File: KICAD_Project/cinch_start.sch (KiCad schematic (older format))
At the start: 14 parts, among them P10 CONN_1, P11 CONN_1, P12 CONN_1, P13 CONN_1, P14 CONN_1, P15 CONN_1, P16 CONN_1, P6 CONN_1, P7 CONN_1, P8 CONN_1, P9 CONN_1, T1 ACT45B

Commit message: Started laying out the harness in DXF, initial schematic capture complete, except for harness.
Signed-off-by: Jared Harvey <TortiseGIT@jaredharvey.com>
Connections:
- net labels added: GND_PWR4, GND_PWR5, GND_PWR6, GND_PWR7, GND_PWR8, INJ00_PIN, INJ01_PIN, INJ02_PIN, INJ03_PIN, INJ04_PIN, INJ05_PIN, INJ06_PIN, INJ07_PIN, INJ08_PIN, INJ09_PIN, INJ13_PIN, INJ14_PIN, INJ15_PIN, INJ16_PIN, INJ17_PIN, INJ18_PIN, INJ19_PIN, INJ20_PIN, INJ21_PIN, INJ22_PIN, INJ23_PIN
- wire segments 375 -> 356

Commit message: About to runs scripts to scrub the BOM's, so here's a backup copy in case it goes wrong.
Signed-off-by: Jared Harvey <TortiseGIT@jaredharvey.com>
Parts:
- R101: renamed from R1; footprint SM0805-R4 -> SM0805
- renumbered D1 to D101, P6 to P101, P7 to P102, P8 to P103, P9 to P104, P10 to P105, P11 to P106, P12 to P107, P13 to P108, P14 to P109, P15 to P110, P16 to P111, T1 to T101
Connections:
- net labels added: AN0, AN1, AN2, AN3, AN4, AN5, AN6, AN7, GND_INJIGN1, GND_INJIGN2, GND_INJING0, GND_INJS3, P0, P1, P2
- net labels removed: AN37_PIN, AN38_PIN, AN39_PIN, GND_PWR4, GND_PWR5, GND_PWR6, GND_PWR8
- wire segments 356 -> 368

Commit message: harness connector is much more ironed out now. CPU is not connected.
Signed-off-by: Jared Harvey <TortiseGIT@jaredharvey.com>
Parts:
- added P101, P113, P114, P115, P116: CONN_1, PINTST, symbol CONN_1
- renumbered P101 to P102, P102 to P103, P103 to P104, P104 to P105, P105 to P106, P106 to P107, P107 to P108, P108 to P109, P109 to P110, P110 to P111, P111 to P112
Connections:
- net labels added: 3.3V_CPU, 5V_CPU, CAM+, CAM-, CANH, CANL, CRANK+, CRANK-, D5, D8, ENG_TEMP, GND1_INJIGN, GND2_INJIGN, GND3_INJIGN, GND4_STAGED8, GND5_STAGED4, GND6_MISC, HS1_12VECU, HS2, HS3, IGN01, IGN02, IGN03, IGN04, IGN05, IGN06, IGN07, IGN08, IGN09, IGN10, IGN11, IGN12, INJ01, INJ02, INJ03, INJ04, INJ05, INJ06, INJ07, INJ08, INJ09, INJ10, INJ11, INJ12, INJ13, INJ14, INJ15, INJ16, INJ17, INJ18, INJ19, INJ20, INJ21, INJ22, INJ23, INJ24, KNCK1+, KNCK1-, KNCK2+, KNCK2-, LB+_WHEEL, LB-_WHEEL, LF+_WHEEL, LF-_WHEEL, MAIT, MAP+_5V, MAP-_GND, MISC_1A, O2_1IA, O2_1IP, O2_1UN, O2_1VM, O2_2IA, O2_2IP, O2_2UN, O2_2VM, P01, P02, P03, P04, P05, P06, P07, P08, P09, P10, P11, P12, P13, P14, RB+_WHEEL, RB-_WHEEL, RF+_WHEEL, RF-_WHEEL, S1, S4, TPS+_5V, TPS-_GND
- net labels removed: 3.3V, 3.3V_CONST, 5V_POWER, AN0, AN1, AN2, AN3, AN32_PIN, AN33_PIN, AN34_PIN, AN35_PIN, AN36_PIN, AN4, AN5, AN6, AN7, CANH-PIN, CANL-PIN, D5_PIN, D8_PIN, GND_INJIGN1, GND_INJIGN2, GND_INJING0, GND_INJS3, GND_PWR1, GND_PWR2, GND_PWR3, GND_PWR7, GND_SENSE, HS0_PIN, HS3_PIN, IGN11_PIN, IGN12_PIN, IGN1_PIN, IGN3_PIN, IGN4_PIN, IGN5_PIN, IGN7_PIN, IGN8_PIN, IGN9_PIN, ING10_PIN, ING2_PIN, ING6_PIN, INJ00_PIN, INJ01_PIN, INJ02_PIN, INJ03_PIN, INJ04_PIN, INJ05_PIN, INJ06_PIN, INJ07_PIN, INJ08_PIN, INJ09_PIN, INJ10_PIN, INJ11_PIN, INJ12_PIN, INJ13_PIN, INJ14_PIN, INJ15_PIN, INJ16_PIN, INJ17_PIN, INJ18_PIN, INJ19_PIN, INJ1_PIN, INJ20_PIN, INJ21_PIN, INJ22_PIN, INJ23_PIN, INJ2_PIN, INJ3_PIN, INJ4_PIN, INJ5_PIN, INJ6_PIN, INJ7_PIN, INJ8_PIN, INJ9_PIN, KNCK1+PIN, KNCK1-PIN, KNCK2+PIN, KNCK2-PIN, MISC3_800, MISC4_800, O2_1IA-PIN, O2_1IP-PIN, O2_1UN-PIN, O2_1VM-PIN, O2_2IA-PIN, O2_2IP-PIN, O2_2UN-PIN, O2_2VM-PIN, P0, P1, P2, S1_PIN, S4_PIN, SWITCHED 12V, THERM1+PIN, THERM2+PIN, THERM_AIR+PIN, THERM_ENG+PIN, VR+_CAM1_PIN, VR+_CAM2_PIN, VR+_CRK1_PIN, VR+_CRK2_PIN, VR+_CR_PIN, VR+_WHBL_PIN, VR+_WHBR_PIN, VR+_WHFL_PIN, VR+_WHFR_PIN, VR+_WHLB_PIN, VR+_WHRB_PIN, VR+_WHRF_PIN, VR-_CAM1_PIN, VR-_CAM2_PIN, VR-_CRK1_PIN, VR-_CRK2_PIN, VR-_CR_PIN, VR-_WHLB_PIN, VR-_WHLF_PIN, VR-_WHRB_PIN, VR-_WHRF_PIN, VR-_WH_COM
- wire segments 368 -> 409
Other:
- note added: "NOTES TO REMEMBER\n\nPERHAPS INSTALL USB FROM PUMA\n"
- note removed: "NOT DONE YET\nNEEDS WORK"
- note removed: "NOTES TO REMEMBER\n\nUPDATE HARNESS CONNECTOR PINOUT\nFINISH INJECTOR/IGNITION CIRCUITS\nPERHAPS INSTALL USB FROM PUMA\n"

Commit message: several pins on the SOM are now connected.
Signed-off-by: Jared Harvey <TortiseGIT@jaredharvey.com>
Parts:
- added P106, P107, P108, P109, P110, P111, P112, P124, P125: CONN_1, PINTST, symbol CONN_1
- renumbered P113 to P102, P114 to P103, P115 to P104, P116 to P105, P102 to P113, P103 to P114, P104 to P115, P105 to P116, P106 to P117, P107 to P118, P108 to P119, P109 to P120, P110 to P121, P111 to P122, P112 to P123
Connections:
- wire segments 409 -> 432
- no-connect marks 21 -> 15

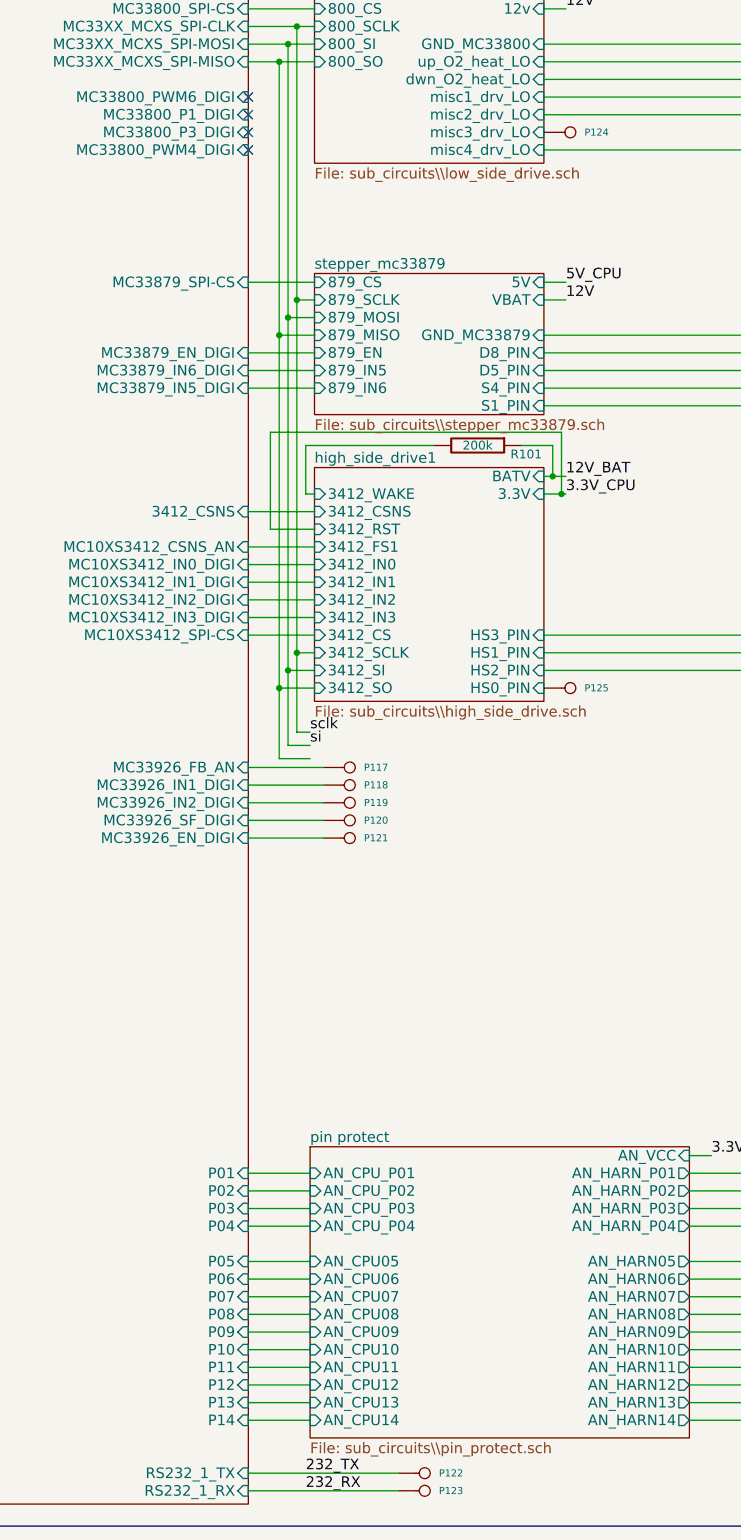
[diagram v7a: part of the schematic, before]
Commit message: Errr, routing doesn't begin yet. Still need to iron our CPU sheet.
Signed-off-by: Jared Harvey <TortiseGIT@jaredharvey.com>
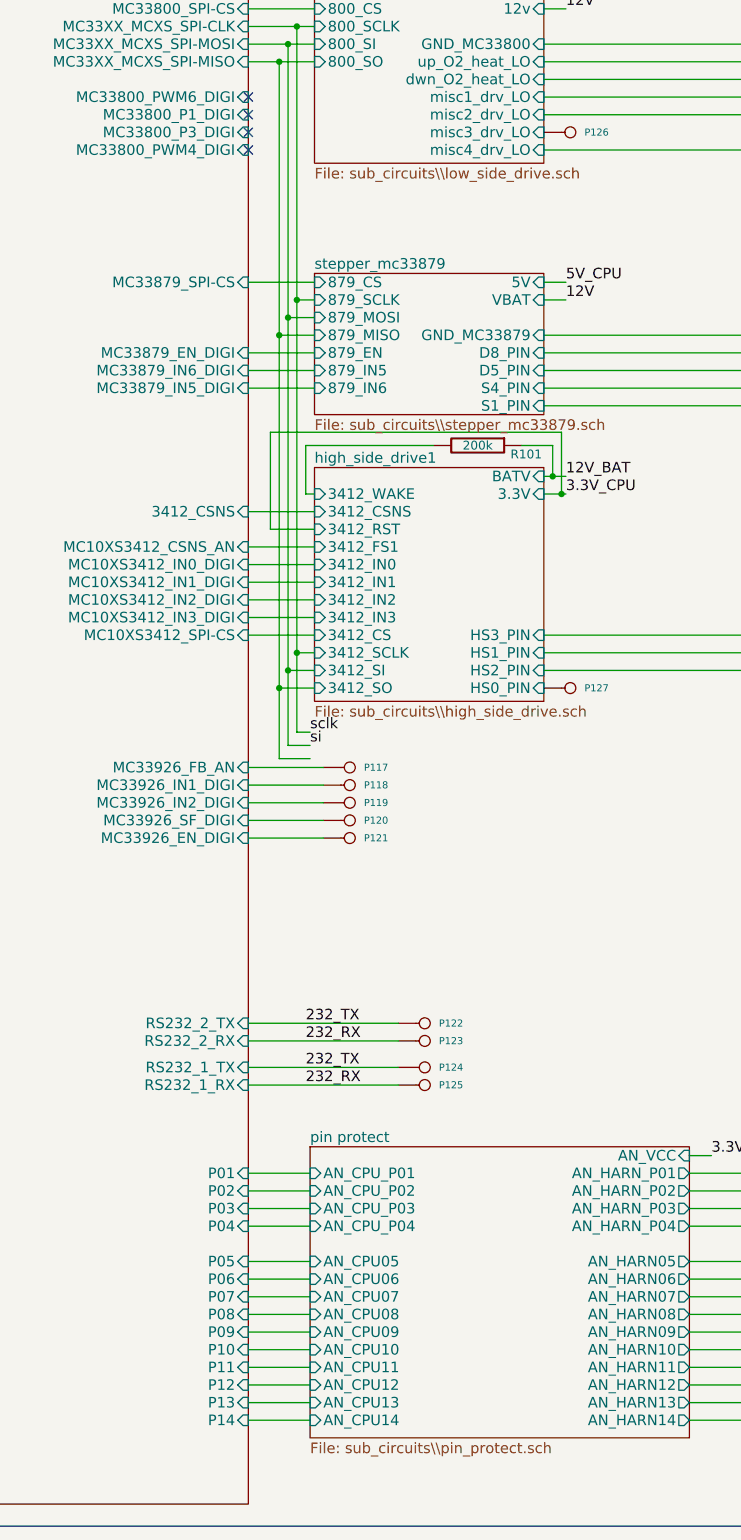
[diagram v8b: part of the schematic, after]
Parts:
- added P122, P123: CONN_1, PINTST, symbol CONN_1
- renumbered P122 to P124, P123 to P125, P124 to P126, P125 to P127
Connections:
- net 232_RX: now also P123.1
- net 232_TX: now also P122.1
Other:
- moved on the sheet: P124, P125
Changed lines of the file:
@@
-EESchema Schematic File Version 2  date 8/20/2011 7:59:49 PM
+EESchema Schematic File Version 2  date 8/20/2011 10:47:21 PM
 LIBS:power
 LIBS:device
@@
 Sheet 1 13
 Title "freeEMS PLUS from Cinch template "
-Date "20 aug 2011"
+Date "21 aug 2011"
 Rev "A-DRAF"
 Comp "diyefi.org/openecu.info"
@@
 Comment4 ""
 $EndDescr
+$Comp
+L CONN_1 P123
+U 1 1 4E506FF2
+P 13700 13625
+F 0 "P123" H 13780 13625 40  0000 L CNN
+F 1 "CONN_1" H 13700 13680 30  0001 C CNN
+F 2 "PINTST" H 13700 13625 60  0001 C CNN
+	1    13700 13625
+	1    0    0    1
+$EndComp
+$Comp
+L CONN_1 P122
+U 1 1 4E506FF1
+P 13700 13525
+F 0 "P122" H 13780 13525 40  0000 L CNN
+F 1 "CONN_1" H 13700 13580 30  0001 C CNN
+F 2 "PINTST" H 13700 13525 60  0001 C CNN
+	1    13700 13525
+	1    0    0    1
+$EndComp
+Text Label 13025 13525 0    60   ~ 0
+232_TX
+Text Label 13025 13625 0    60   ~ 0
+232_RX
+Wire Wire Line
+	13550 13525 12700 13525
+Wire Wire Line
+	13550 13625 12700 13625
 $Comp
 L CONN_1 P109
@@
 $EndComp
 $Comp
-L CONN_1 P124
+L CONN_1 P126
 U 1 1 4E4F9546
 P 14525 8475
-F 0 "P124" H 14605 8475 40  0000 L CNN
+F 0 "P126" H 14605 8475 40  0000 L CNN
 F 1 "CONN_1" H 14525 8530 30  0001 C CNN
 F 2 "PINTST" H 14525 8475 60  0001 C CNN
@@
 $EndComp
 $Comp
-L CONN_1 P125
+L CONN_1 P127
 U 1 1 4E4F9534
 P 14525 11625
-F 0 "P125" H 14605 11625 40  0000 L CNN
+F 0 "P127" H 14605 11625 40  0000 L CNN
 F 1 "CONN_1" H 14525 11680 30  0001 C CNN
 F 2 "PINTST" H 14525 11625 60  0001 C CNN
@@
 	5050 3500 4425 3500
 Wire Wire Line
-	13550 16175 12700 16175
-Wire Wire Line
-	13550 16075 12700 16075
+	13550 13875 12700 13875
+Wire Wire Line
+	13550 13775 12700 13775
 Wire Wire Line
 	7100 12325 7875 12325
@@
 F35 "CJ125_2_SPI-CS" I L 9825 9675 60
 F36 "CJ125_1_SPI-CS" I L 9825 8675 60
-F37 "RS232_1_RX" I R 12700 16175 60
-F38 "RS232_1_TX" I R 12700 16075 60
+F37 "RS232_1_RX" I R 12700 13875 60
+F38 "RS232_1_TX" I R 12700 13775 60
 F39 "TJA1054_2_CAN_RX" I L 9825 15900 60
 F40 "TJA1054_1_CAN_TX" I L 9825 15800 60
@@
 F126 "P02" I R 12700 14475 60
 F127 "09_IGN_DIGI" I R 12700 6500 60
+F128 "RS232_2_TX" I R 12700 13525 60
+F129 "RS232_2_RX" I R 12700 13625 60
 $EndSheet
 $Comp
@@
 Text Label 6900 7050 2    60   ~ 0
 232_RX
-Text Label 13025 16175 0    60   ~ 0
+Text Label 13025 13875 0    60   ~ 0
 232_RX
-Text Label 13025 16075 0    60   ~ 0
+Text Label 13025 13775 0    60   ~ 0
 232_TX
 Entry Wire Line
@@
 TPS_AN
 $Comp
-L CONN_1 P122
+L CONN_1 P124
 U 1 1 4C1CA4B7
-P 13700 16075
-F 0 "P122" H 13780 16075 40  0000 L CNN
-F 1 "CONN_1" H 13700 16130 30  0001 C CNN
-F 2 "PINTST" H 13700 16075 60  0001 C CNN
-	1    13700 16075
+P 13700 13775
+F 0 "P124" H 13780 13775 40  0000 L CNN
+F 1 "CONN_1" H 13700 13830 30  0001 C CNN
+F 2 "PINTST" H 13700 13775 60  0001 C CNN
+	1    13700 13775
 	1    0    0    1
 $EndComp
 $Comp
-L CONN_1 P123
+L CONN_1 P125
 U 1 1 4C1CA4B6
-P 13700 16175
-F 0 "P123" H 13780 16175 40  0000 L CNN
-F 1 "CONN_1" H 13700 16230 30  0001 C CNN
-F 2 "PINTST" H 13700 16175 60  0001 C CNN
-	1    13700 16175
+P 13700 13875
+F 0 "P125" H 13780 13875 40  0000 L CNN
+F 1 "CONN_1" H 13700 13930 30  0001 C CNN
+F 2 "PINTST" H 13700 13875 60  0001 C CNN
+	1    13700 13875
 	1    0    0    1
 $EndComp
